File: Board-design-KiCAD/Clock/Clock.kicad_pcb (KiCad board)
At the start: 2 copper layers, 43 parts, among them M1 SevSeg4Inch, M2 SevSeg4Inch, Y1 SevSeg1.8Inch, Y2 SevSeg1.8Inch, Y3 SevSeg1.8Inch, Y4 SevSeg1.8Inch

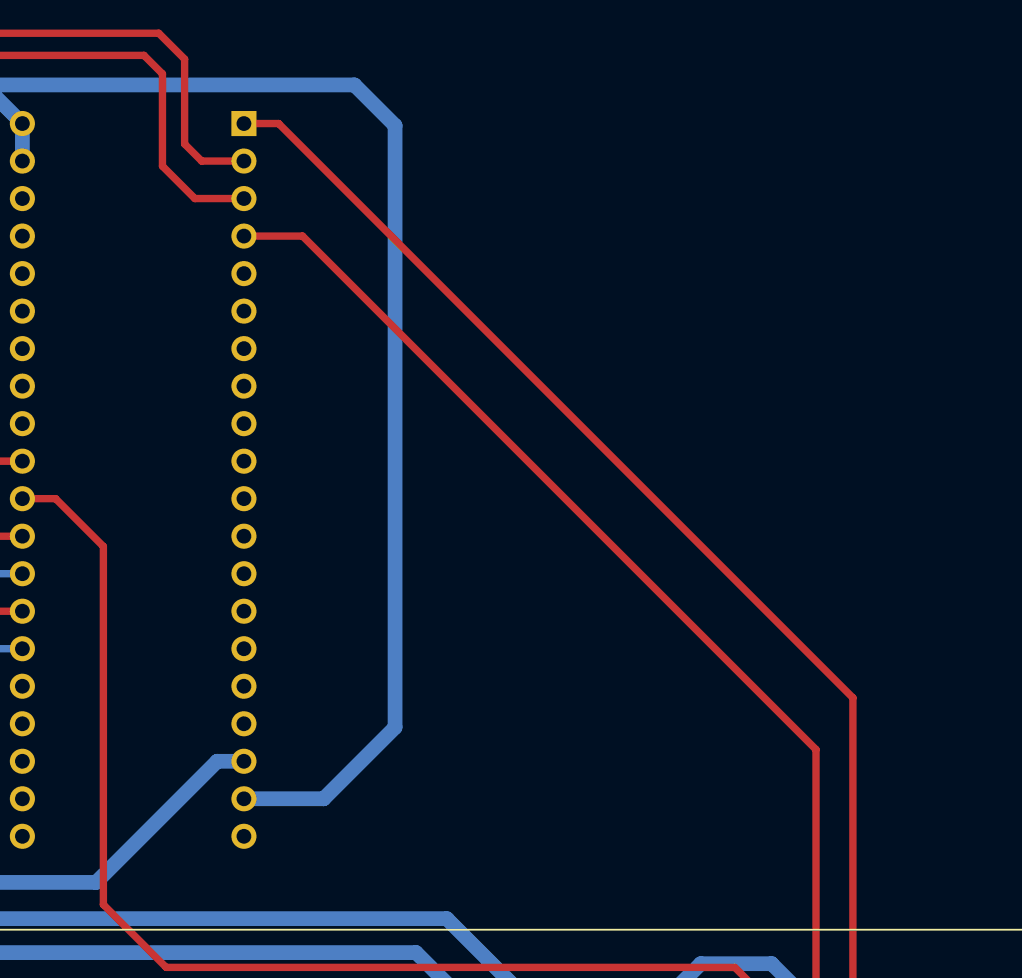
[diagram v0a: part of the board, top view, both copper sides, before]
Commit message: Finish integrating WiFi and RTC
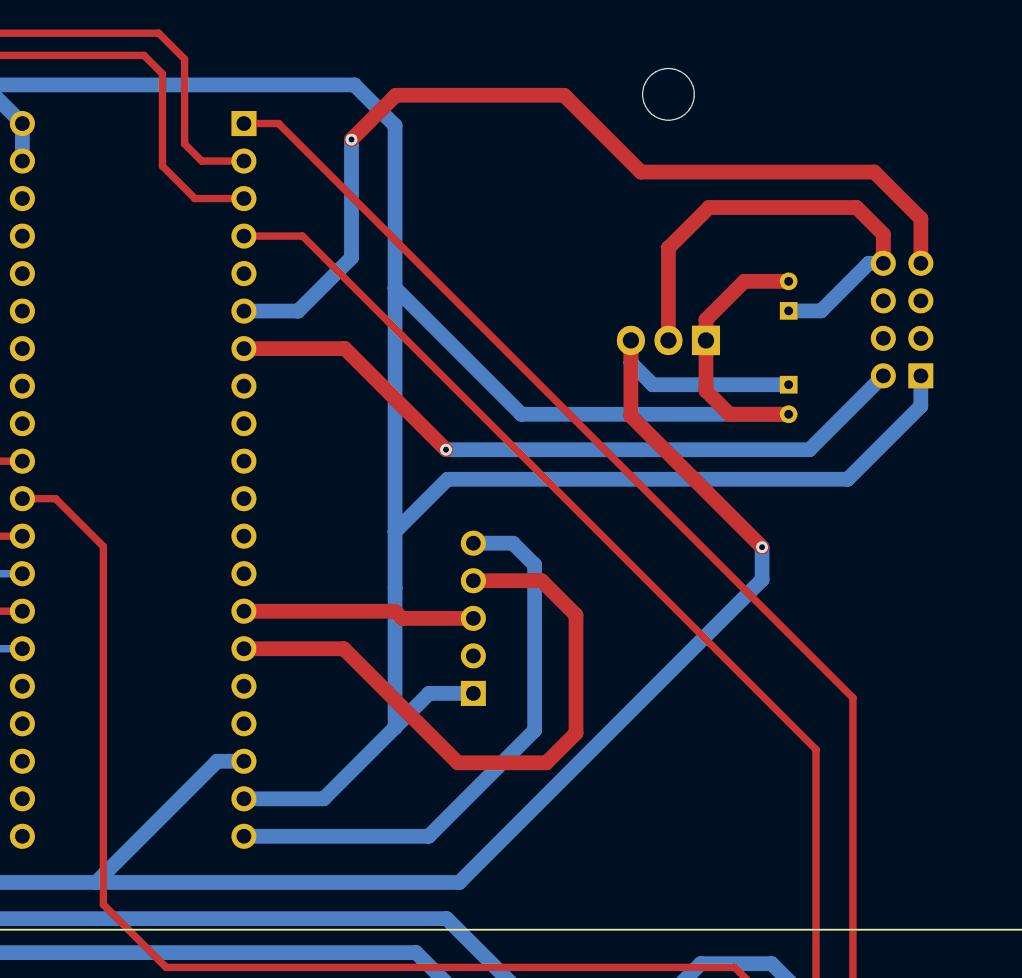
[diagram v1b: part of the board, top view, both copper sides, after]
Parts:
- added 3.3V-Cin1: CP1, Capacitor_THT:CP_Radial_D4.0mm_P2.00mm, B.Cu at (529.4, 89.8)
- added 3.3V-Cout1: CP1, Capacitor_THT:CP_Radial_D4.0mm_P2.00mm, B.Cu at (529.4, 84.8)
- added MCU_2: Generic-ESP8266, Custom:Generic-ESP8266, B.Cu at (546.8, 85.4)
- added RTC1: DS3231-RPi, Custom:DS3231-RPi, B.Cu at (514.2, 105.6)
- added Regulator-3.3V1: LM1117-3.3, Package_TO_SOT_THT:TO-220-3_Horizontal_TabDown, B.Cu at (523.8, 86.8)
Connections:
- MCU_1 pad 14: Net-(MCU_1-Pad14) -> RTC_SCL
- MCU_1 pad 15: Net-(MCU_1-Pad15) -> RTC_SDA
- MCU_1 pad 20: Net-(MCU_1-Pad20) -> +3.3V
- MCU_1 pad 6: Net-(MCU_1-Pad6) -> STM32TX-EPS8266RX
- MCU_1 pad 7: Net-(MCU_1-Pad7) -> STM32RX-EPS8266TX
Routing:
- net GND: track 1372.8 -> 1468.2 mm
- net +5V: track 704.6 -> 790.9 mm, vias 7 -> 8
- net STM32TX-EPS8266RX: track 0.00 -> 63.1 mm, vias 0 -> 1
- net STM32RX-EPS8266TX: track 0.00 -> 48.2 mm, vias 0 -> 1
- net RTC_SDA: track 0.00 -> 42.4 mm
- net +3.3V: track 0.00 -> 38.6 mm
- net Net-(3.3V-Cout1-Pad1): track 0.00 -> 32.4 mm
- net RTC_SCL: track 0.00 -> 15.7 mm

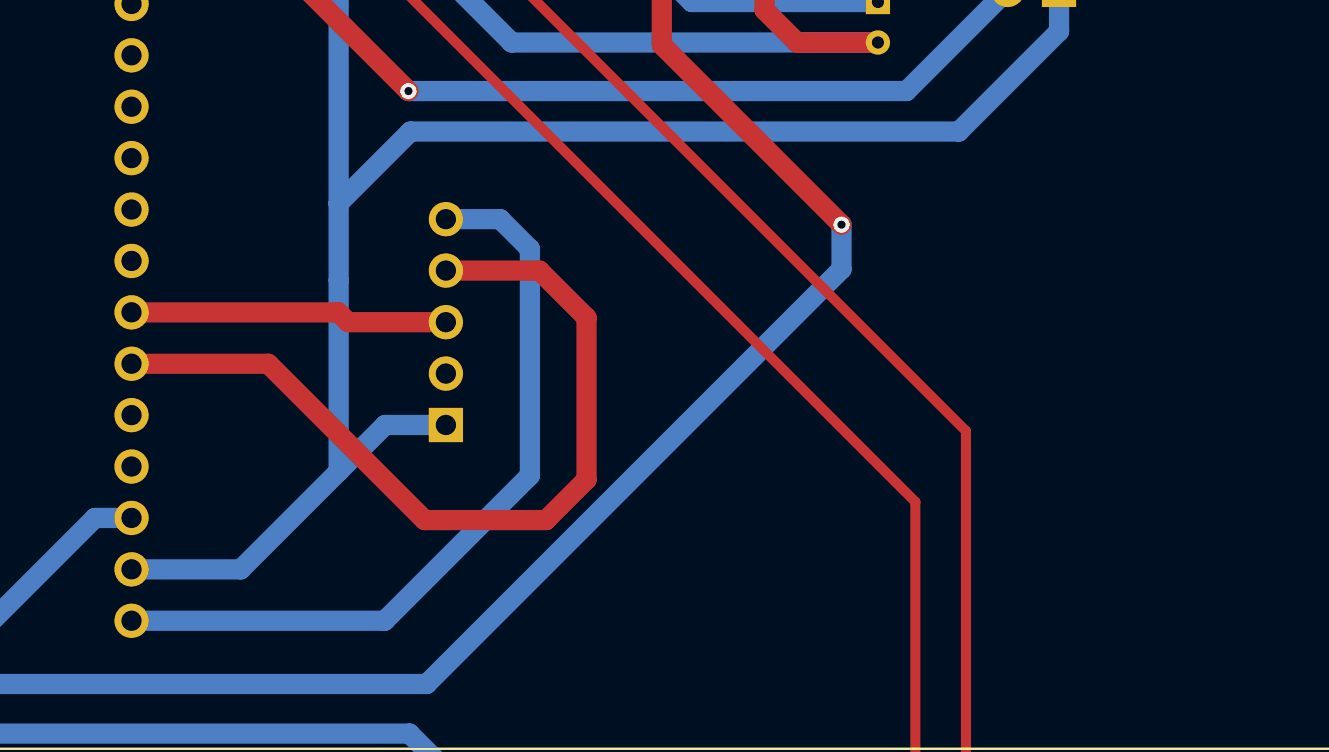
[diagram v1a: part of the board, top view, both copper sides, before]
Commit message: Update part(s): DS3231 RTC Module
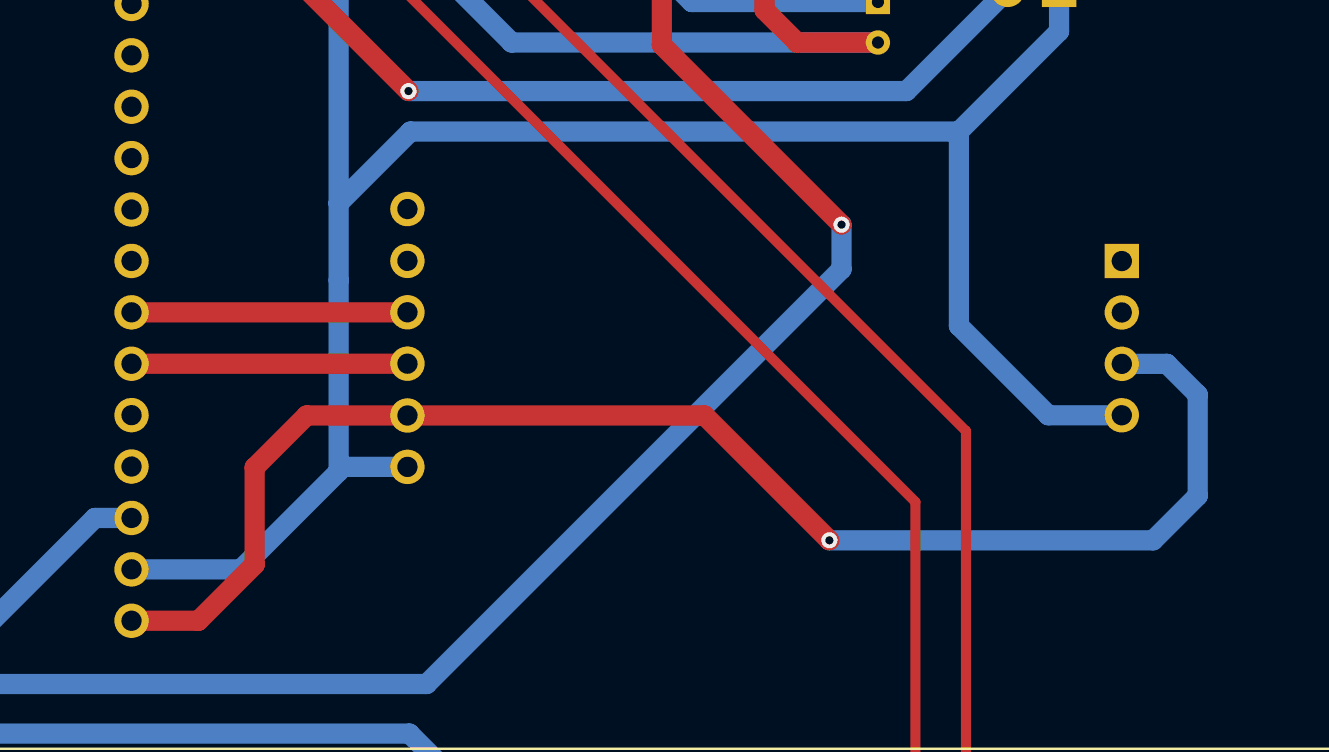
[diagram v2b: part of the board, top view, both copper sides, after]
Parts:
- RTC1: value DS3231-RPi -> DS3231-Module; footprint Custom:DS3231-RPi -> Custom:DS3231-Module
- moved RTC1 9.63 mm to (523.8, 106.4), turned to 270 degrees
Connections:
- RTC1 pad 1: GND -> Net-(RTC1-Pad1)
- RTC1 pad 3: RTC_SCL -> +3.3V
- RTC1 pad 4: RTC_SDA -> GND
- RTC1 pad 5: +3.3V -> GND
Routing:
- net +3.3V: track 38.6 -> 72.5 mm, vias 0 -> 1
- net RTC_SDA: track 42.4 -> 13.6 mm
- net GND: track 1468.2 -> 1484.9 mm
- net RTC_SCL: track 15.7 -> 13.6 mm

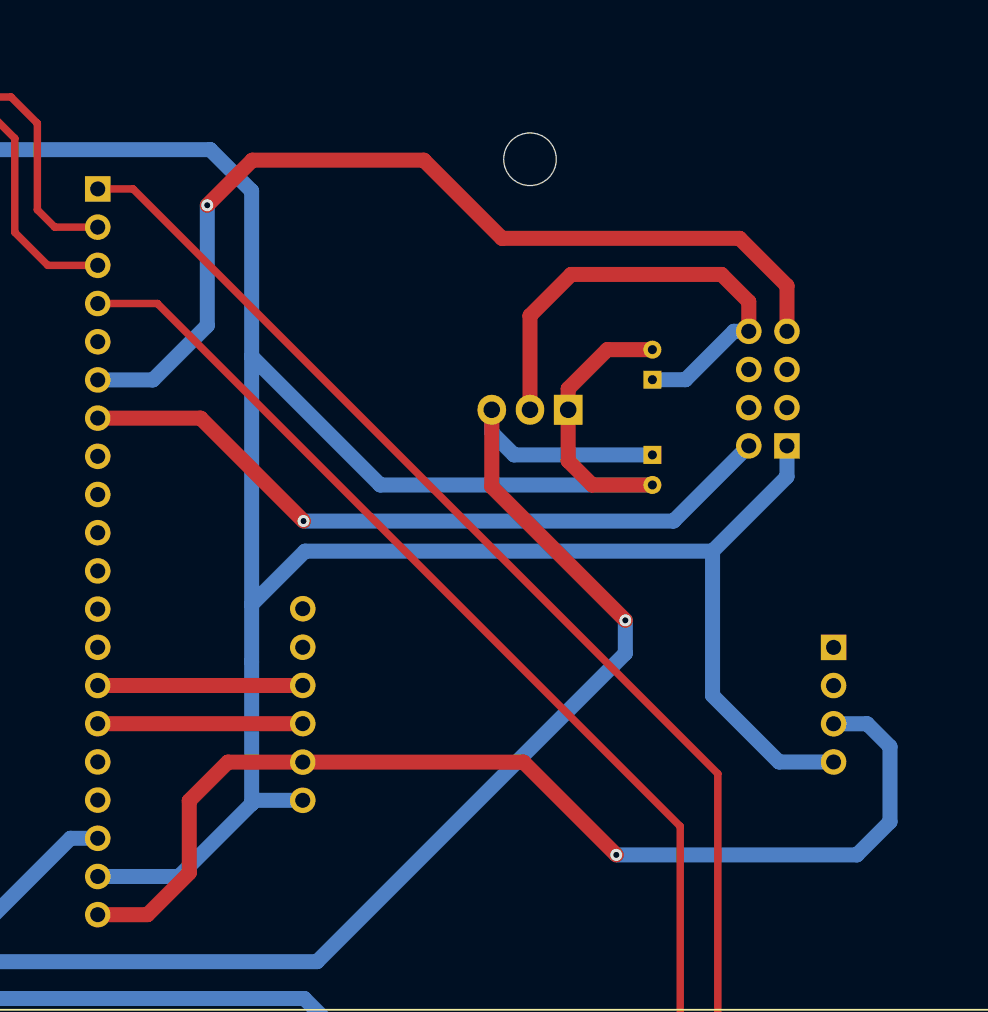
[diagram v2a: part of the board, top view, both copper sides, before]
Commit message: Add credential reset button for ESP8266
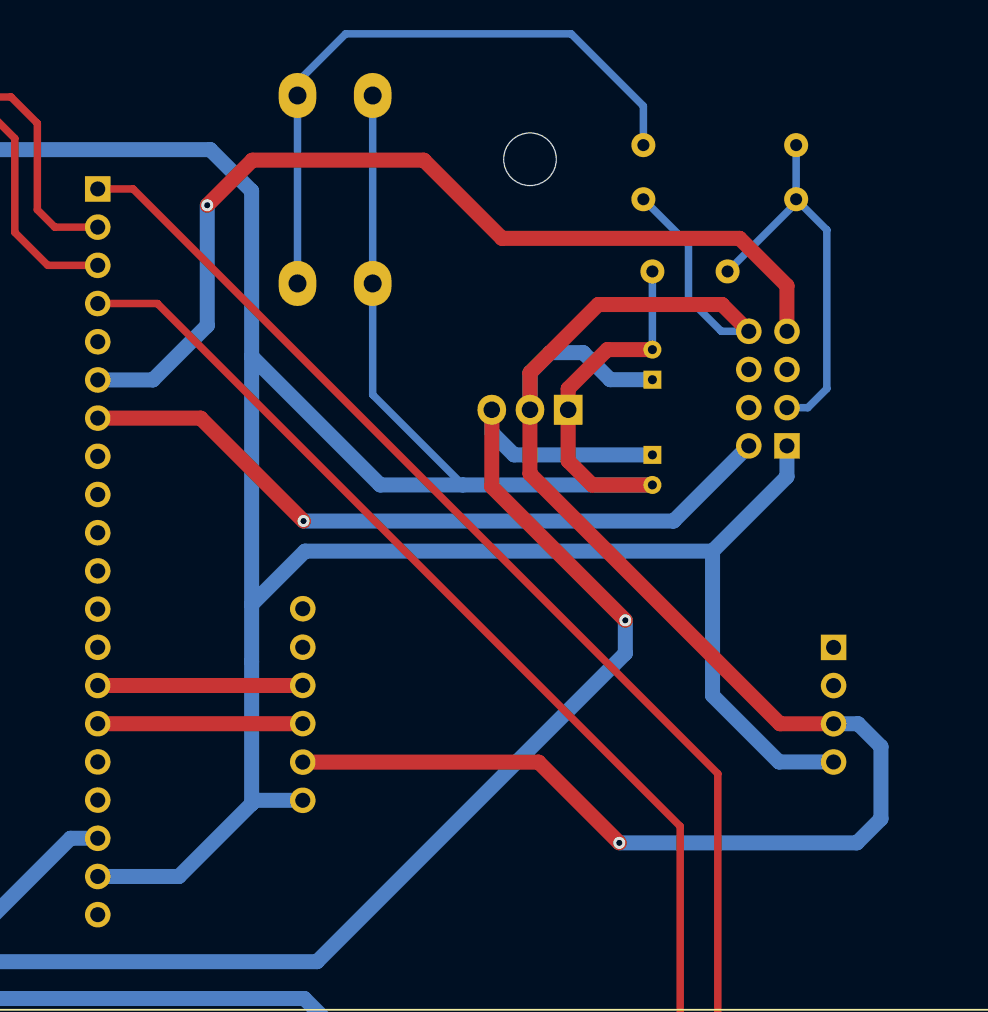
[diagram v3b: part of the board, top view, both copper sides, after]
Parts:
- added Credentials_Reset1: SW_Push_Dual_Custom, Button_Switch_THT:SW_PUSH-12mm_Wuerth-430476085716, B.Cu at (510.8, 78.4)
- added Debounce1: 10nF, Capacitor_THT:C_Disc_D5.0mm_W2.5mm_P5.00mm, B.Cu at (534.4, 77.6)
- added R_BUTTON1: 1k, Resistor_THT:R_Axial_DIN0207_L6.3mm_D2.5mm_P10.16mm_Horizontal, B.Cu at (528.8, 69.2)
- added R_PULLUP1: 10k, Resistor_THT:R_Axial_DIN0207_L6.3mm_D2.5mm_P10.16mm_Horizontal, B.Cu at (528.8, 72.8)
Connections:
- 3.3V-Cout1 pad 1: Net-(3.3V-Cout1-Pad1) -> +3.3V
- MCU_1 pad 20: +3.3V -> Net-(MCU_1-Pad20)
- MCU_2 pad 3: Net-(MCU_2-Pad3) -> CredentialsReset
- MCU_2 pad 8: Net-(3.3V-Cout1-Pad1) -> +3.3V
- Regulator-3.3V1 pad 2: Net-(3.3V-Cout1-Pad1) -> +3.3V
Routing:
- net +3.3V: track 72.5 -> 125.5 mm
- net Net-(Credentials_Reset1-Pad2): track 0.00 -> 42.3 mm
- net GND: track 1484.9 -> 1518.5 mm
- net Net-(3.3V-Cout1-Pad1): track 32.4 -> 0.00 mm
- net CredentialsReset: track 0.00 -> 26.9 mm

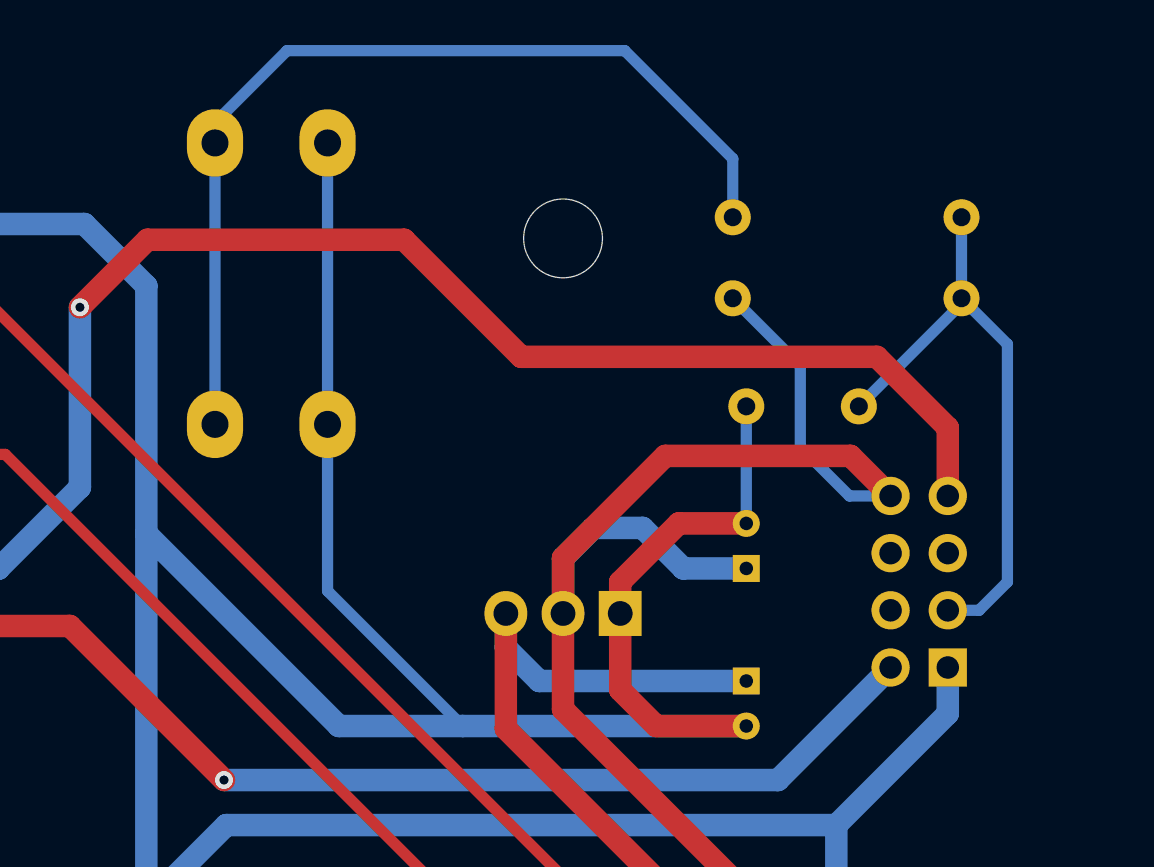
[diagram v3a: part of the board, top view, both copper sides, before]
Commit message: Modify button circuit and build code for button management.
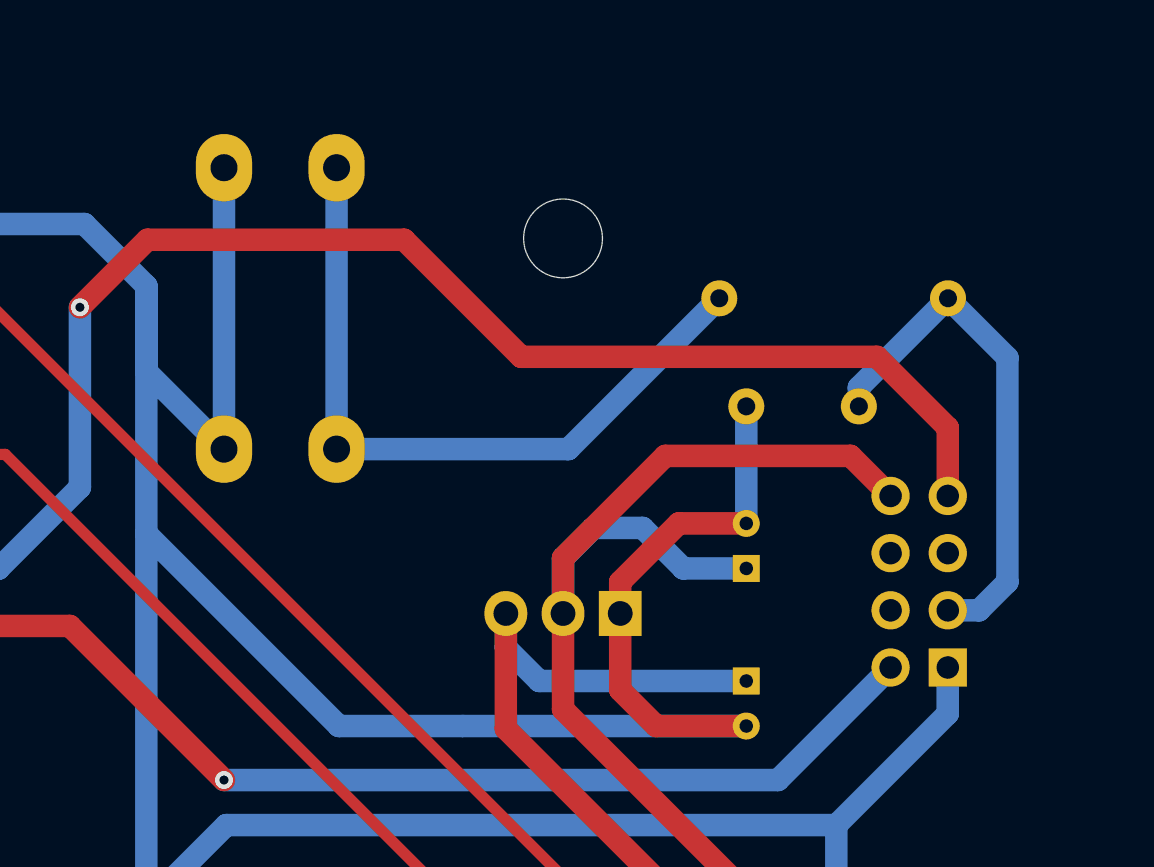
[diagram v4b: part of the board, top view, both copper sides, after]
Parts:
- removed R_PULLUP1: 10k, Resistor_THT:R_Axial_DIN0207_L6.3mm_D2.5mm_P10.16mm_Horizontal
- moved Credentials_Reset1 12.3 mm to (506.2, 67.0), turned to 270 degrees
- moved R_BUTTON1 3.65 mm to (528.2, 72.8)
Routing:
- net +3.3V: track 125.5 -> 112.8 mm
- net Net-(Credentials_Reset1-Pad2): track 42.3 -> 32.3 mm
- net GND: track 1518.5 -> 1511.3 mm
- net CredentialsReset: track 26.9 -> 23.3 mm
